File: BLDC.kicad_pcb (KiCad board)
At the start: 4 copper layers, 60 x 60 mm, 131 parts, among them J1 43650-0510, J2 436500313, J3 DNP, J4 43650-0510, J5 BONUS, U1 LMZ21700SIL, U12 MCP9808, U13 AS5047U, U17 INA250, U18 INA250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

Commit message: a bit of trivial cleanup. sent out for quote
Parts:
- moved TP3 0.42 mm to (151.1, 99.9)
- moved TP4 0.28 mm to (149.5, 98.6)
- moved TP6 0.14 mm to (146.5, 98.4)
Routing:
- net GND: track 138.8 -> 137.3 mm, vias 118 -> 119

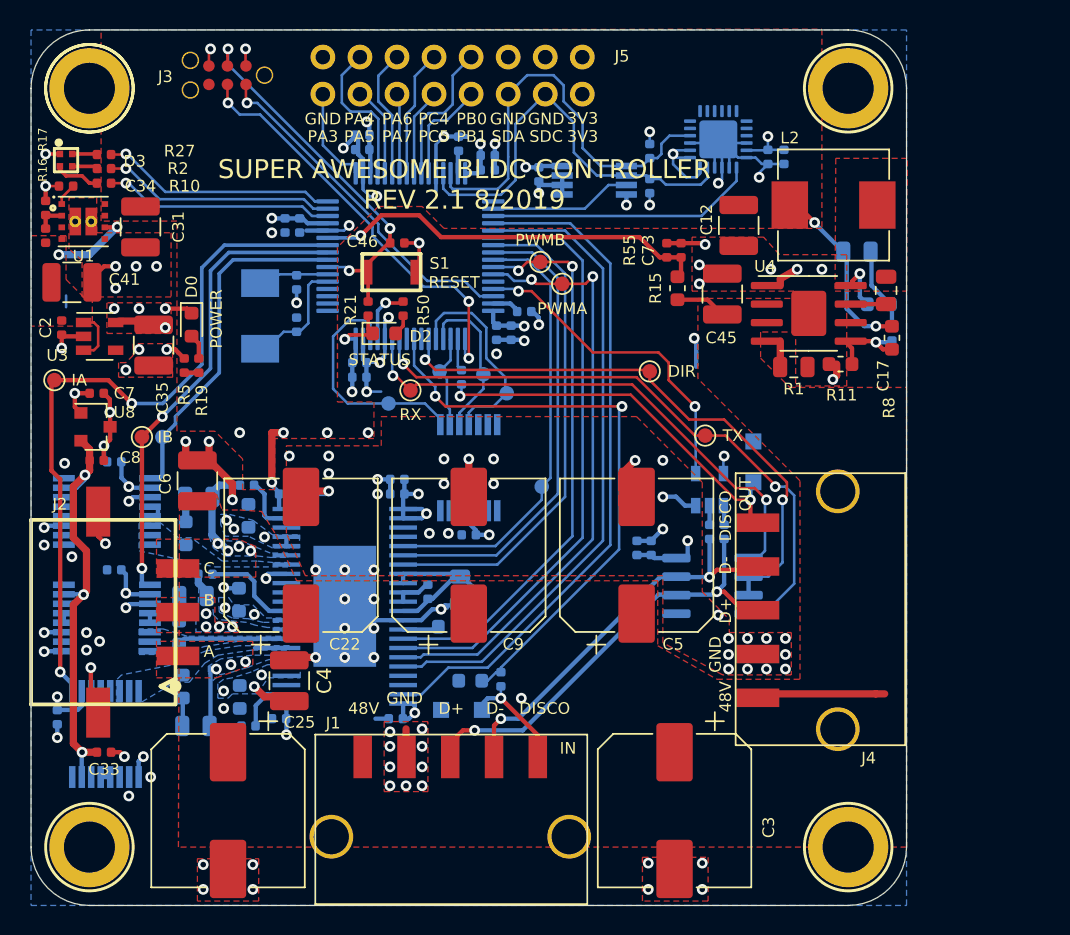
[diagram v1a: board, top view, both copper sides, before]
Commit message: WIP new revision, change INA250 to INA253 (higher bandwidth), regulator to low EMI version
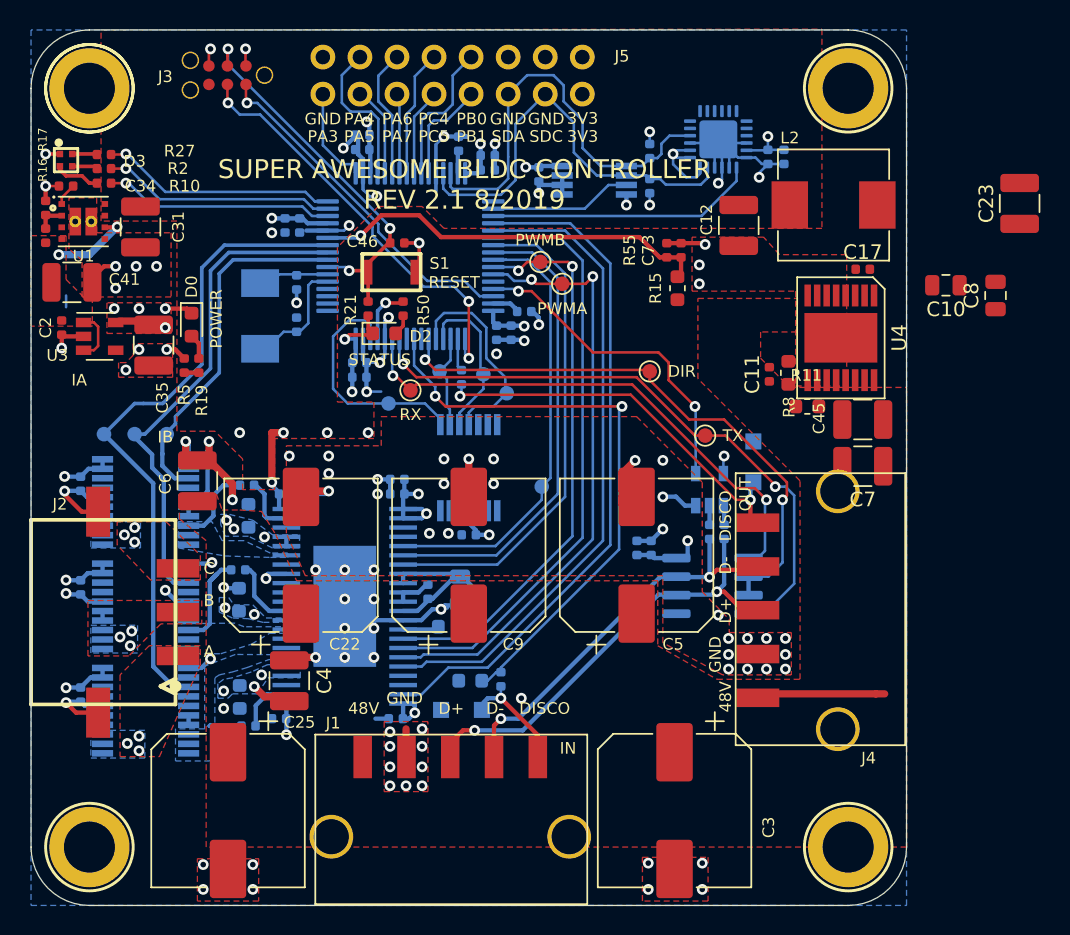
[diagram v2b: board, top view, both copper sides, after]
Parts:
- removed C28, C29: DNP, Capacitor_SMD:C_0603_1608Metric
- removed C33: 1u, Capacitor_SMD:C_0402_1005Metric
- removed R1: 40k2, Resistor_SMD:R_0805_2012Metric
- removed R12, R13, R14: DNP, Resistor_SMD:R_0805_2012Metric
- removed R7: 255k, Resistor_SMD:R_0603_1608Metric
- removed U17, U18, U19: INA250, Package_SO:TSSOP-16_4.4x5mm_P0.65mm
- removed U8: REF3312AIDBZ, Package_TO_SOT_SMD:SOT-23
- added U10: INA253, Package_SO:TSSOP-20_4.4x6.5mm_P0.65mm, B.Cu at (126.3, 121.7)
- added U11: INA253, Package_SO:TSSOP-20_4.4x6.5mm_P0.65mm, B.Cu at (126.3, 114.5)
- added U14: INA253, Package_SO:TSSOP-20_4.4x6.5mm_P0.65mm, B.Cu at (126.3, 107.3)
- C10: value 47p -> 2u2; footprint Capacitor_SMD:C_0402_1005Metric -> Capacitor_SMD:C_0805_2012Metric; moved to F.Cu
- C11: value 2n2 -> 82p; footprint Capacitor_SMD:C_0805_2012Metric -> Capacitor_SMD:C_0402_1005Metric; moved to F.Cu
- C17: value 2n2 -> 470n; footprint Capacitor_SMD:C_0805_2012Metric -> Capacitor_SMD:C_0402_1005Metric
- C23: value DNP -> 22u; footprint Capacitor_SMD:C_0603_1608Metric -> Capacitor_SMD:C_1210_3225Metric; moved to F.Cu
- C7: value 100n -> 4u7; footprint Capacitor_SMD:C_0402_1005Metric -> Capacitor_SMD:C_1210_3225Metric
- C8: value 1u -> 4u7; footprint Capacitor_SMD:C_0402_1005Metric -> Capacitor_SMD:C_0805_2012Metric
- L2: value 82u -> 100u
- R11: value 49k9 -> 92k
- R8: value 453k -> 1M
- TP11, TP12: moved to B.Cu
- U4: value LM5163 -> LM46000; footprint Package_SO:SOIC-8-1EP_3.9x4.9mm_P1.27mm_EP2.41x3.3mm -> BLDC:PWP0016G
- moved C8 62.6 mm to (184.6, 93.2), turned to 90 degrees
- moved C23 61.5 mm to (186.2, 86.9), turned to 90 degrees
- moved C7 52.7 mm to (175.5, 104.9)
- moved C45 12.9 mm to (175.5, 101.7), turned to 180 degrees
- moved C11 10.3 mm to (169.1, 98.6), turned to 90 degrees
- moved R8 7.49 mm to (170.4, 98.5)
- moved TP11 5.02 mm to (123.5, 102.7)
- moved C10 4.96 mm to (181.2, 92.5), turned to 180 degrees
- moved R11 3.69 mm to (171.7, 100.8), turned to 0 degrees
- moved U4 2.77 mm to (174.0, 96.1), turned to 180 degrees
- moved C13 2.75 mm to (121.9, 106.1), turned to 90 degrees
- moved C14 2.59 mm to (121.9, 113.2), turned to 90 degrees
- moved C53 2.27 mm to (132.7, 112.0)
- moved C16 2.23 mm to (121.9, 120.5)
- moved C17 2.16 mm to (175.5, 91.4), turned to 0 degrees
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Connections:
- C10 pad 2: Net-(C10-Pad2) -> GND
- C11 pad 1: +12V -> Net-(C11-Pad1)
- C11 pad 2: Net-(C10-Pad1) -> +12V
- C23 pad 1: Net-(C23-Pad1) -> +12V
- C23 pad 2: /GND_C -> GND
- C7 pad 2: +3V3 -> +48V
- C8 pad 1: GND -> +12V
- C8 pad 2: +1V2 -> GND
- J2 pad 1: /driver_phase-A -> /motor_phase-A
- J2 pad 2: /driver_phase-B -> /motor_phase-B
- J2 pad 3: /driver_phase-C -> /motor_phase-C
- L2 pad 1: Net-(C17-Pad1) -> Net-(C17-Pad2)
- R11 pad 1: Net-(C10-Pad2) -> Net-(C11-Pad1)
- R8 pad 2: Net-(C10-Pad2) -> Net-(C11-Pad1)
- U4 pad 1: GND -> Net-(C17-Pad2)
- U4 pad 2: +48V -> Net-(C17-Pad2)
- U4 pad 3: +48V -> Net-(C17-Pad1)
- U4 pad 4: Net-(R1-Pad1) -> Net-(C10-Pad1)
- U4 pad 5: Net-(C10-Pad2) -> +12V
- U4 pad 6: Net-(U4-Pad6) -> GND
- U4 pad 7: Net-(C17-Pad2) -> Net-(U4-Pad7)
- U4 pad 8: Net-(C17-Pad1) -> Net-(U4-Pad8)
- U4 pad 9: GND -> Net-(C11-Pad1)
- U5 pad 29: /GND_A -> GND
- U5 pad 30: /GND_B -> GND
- U5 pad 38: /GND_C -> GND
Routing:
- net +1V2: track 29.1 -> 0.00 mm, vias 3 -> 0
- net +12V: track 31.3 -> 19.1 mm, vias 11 -> 9
- net /GND_B: track 7.50 -> 0.00 mm
- net Net-(C10-Pad2): track 5.85 -> 0.00 mm, vias 1 -> 0
- net Net-(C10-Pad1): track 5.39 -> 0.00 mm
- net /driver_phase-B: track 1.69 -> 6.99 mm, vias 4 -> 0
- net /ISENSE_A: track 49.7 -> 44.9 mm, vias 2 -> 0
- net /driver_phase-A: track 6.20 -> 2.27 mm, vias 3 -> 0
- net +3V3: track 64.6 -> 61.0 mm, vias 24 -> 23
- net GND: track 137.3 -> 133.7 mm, vias 119 -> 100
- net +48V: track 15.1 -> 11.6 mm
- net Net-(C17-Pad1): track 3.34 -> 0.00 mm, vias 1 -> 0
- net Net-(C17-Pad2): track 2.20 -> 0.00 mm
- net /GND_A: track 2.16 -> 0.00 mm
- net Net-(C29-Pad1): track 1.93 -> 0.00 mm
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- added copper zone on F.Cu, net (none)
- added copper zone on B.Cu, net /motor_phase-A
- added copper zone on F.Cu, net /motor_phase-A
- added copper zone on B.Cu, net /motor_phase-B
- added copper zone on F.Cu, net /motor_phase-B
- added copper zone on B.Cu, net /motor_phase-C
- added copper zone on F.Cu, net /motor_phase-C
- removed copper zone on B.Cu, net /GND_A
- removed copper zone on B.Cu, net /GND_B
- removed copper zone on B.Cu, net /GND_C
- removed copper zone on F.Cu, net /driver_phase-A
- removed copper zone on F.Cu, net /driver_phase-B
- removed copper zone on F.Cu, net /driver_phase-C
- removed copper zone on F.Cu, net Net-(C17-Pad1)

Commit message: tinker with layout, mostly with 12v dc-dc
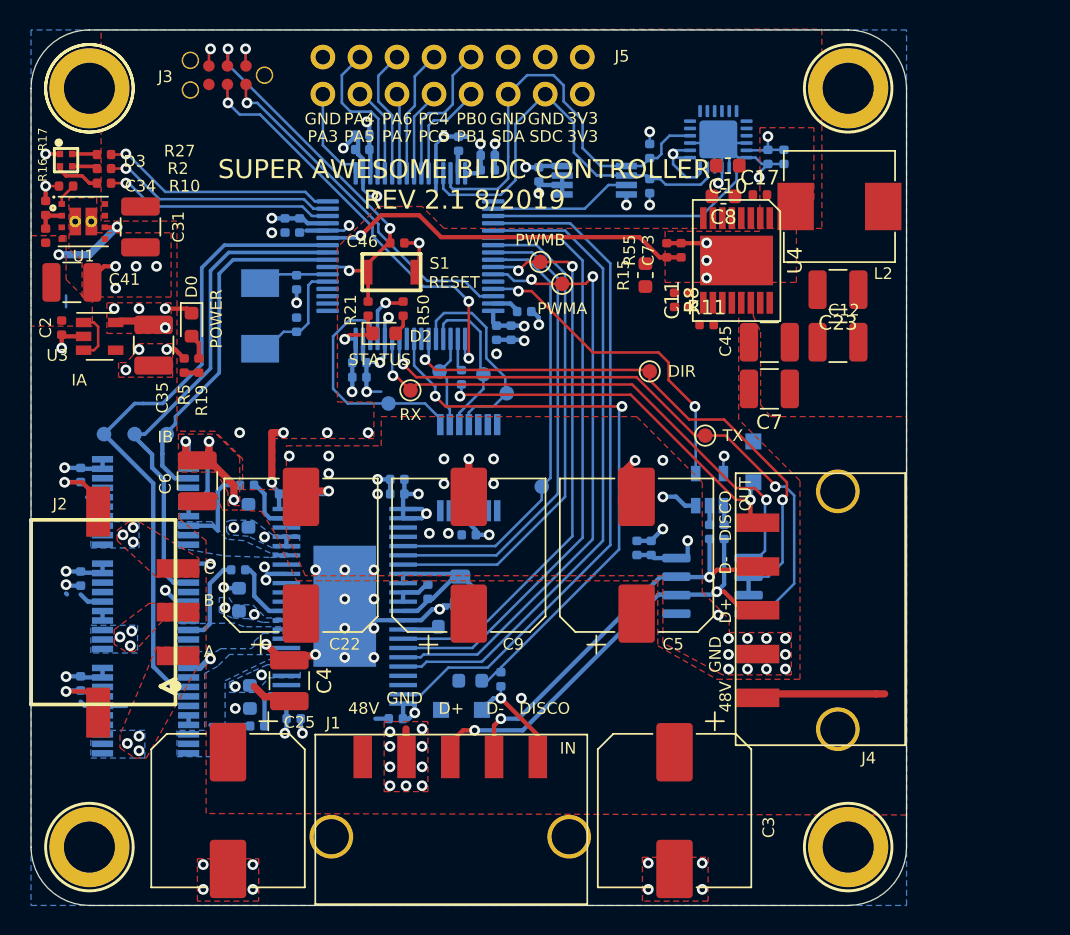
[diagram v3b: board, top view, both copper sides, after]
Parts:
- C10: footprint Capacitor_SMD:C_0805_2012Metric -> Capacitor_SMD:C_0603_1608Metric
- C8: value 4u7 -> 2u2; footprint Capacitor_SMD:C_0805_2012Metric -> Capacitor_SMD:C_0603_1608Metric
- R11, R8: footprint Resistor_SMD:R_0603_1608Metric -> Resistor_SMD:R_0402_1005Metric
- moved C8 19.8 mm to (166.0, 86.4), turned to 180 degrees
- moved C10 17.1 mm to (166.3, 84.3)
- moved C23 13.8 mm to (173.8, 92.8), turned to 180 degrees
- moved C12 10.5 mm to (173.8, 96.4), turned to 180 degrees
- moved R8 9.26 mm to (162.6, 93.5)
- moved U4 8.90 mm to (166.9, 90.8)
- moved R11 8.89 mm to (164.8, 95.2)
- moved C17 8.70 mm to (168.5, 86.3)
- moved C7 8.31 mm to (169.1, 99.6)
- moved C45 8.31 mm to (169.1, 96.4)
- moved C11 7.50 mm to (163.6, 93.5)
- moved R15 2.38 mm to (160.6, 91.8)
- moved C52 1.00 mm to (136.5, 122.2), turned to 180 degrees
- moved C16 0.77 mm to (121.9, 119.8)
- moved C1 0.70 mm to (133.5, 120.7)
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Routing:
- net GND: track 133.7 -> 140.7 mm, vias 100 -> 103
- net /VSENSE_VIN: track 27.6 -> 26.1 mm
- net /driver_phase-C: track 5.49 -> 6.52 mm
- net /driver_phase-B: track 6.99 -> 6.23 mm
- net +3V3: track 61.0 -> 60.3 mm
- net +48V: vias 8 -> 6
- removed copper zone on F.Cu, net (none)

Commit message: Added 3d model for regulator, routed all design (passing DRC)
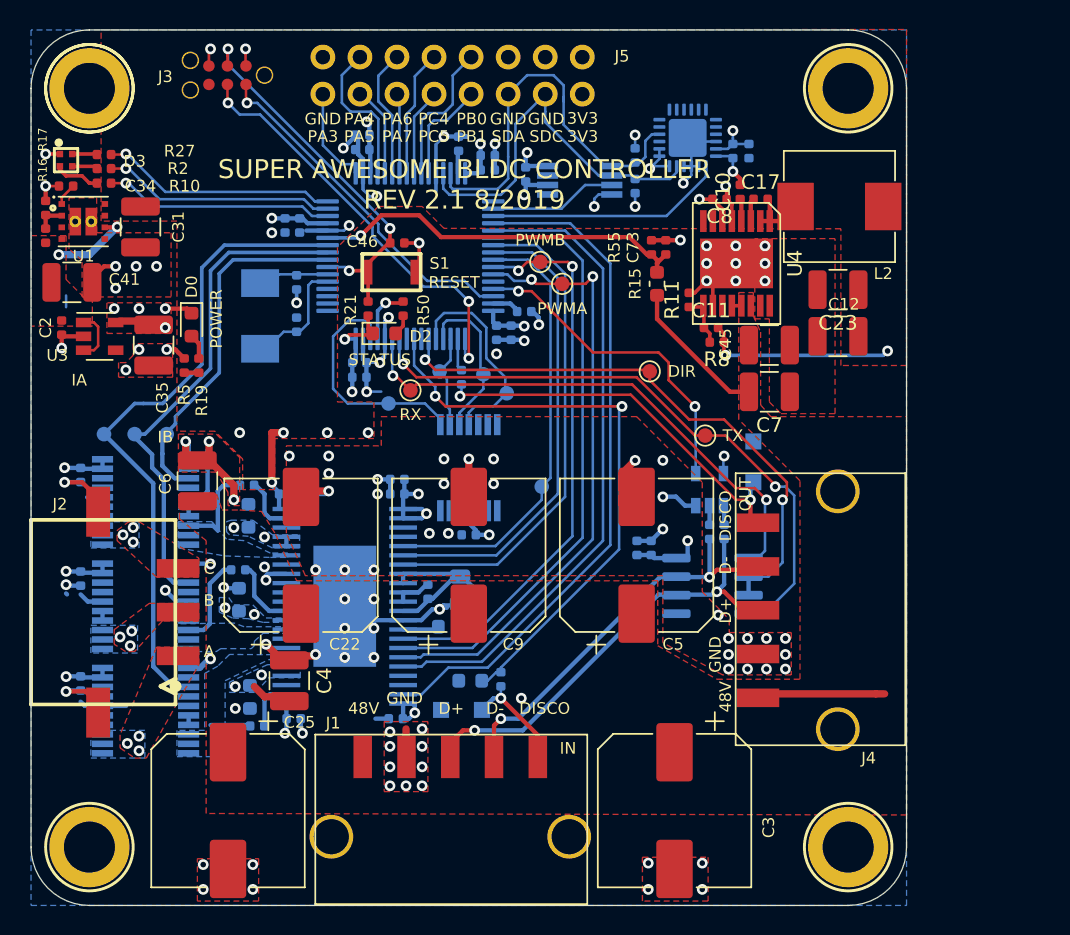
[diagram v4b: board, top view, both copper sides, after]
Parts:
- C10, C8: footprint Capacitor_SMD:C_0603_1608Metric -> Capacitor_SMD:C_0402_1005Metric
- moved R8 4.10 mm to (165.5, 96.4), turned to 180 degrees
- moved C20 2.43 mm to (167.7, 83.3)
- moved C21 2.43 mm to (166.6, 83.3)
- moved C11 2.42 mm to (165.1, 95.4), turned to 0 degrees
- moved U2 2.10 mm to (163.5, 82.4)
- moved R11 2.08 mm to (163.6, 93.5), turned to 90 degrees
- moved C10 1.99 mm to (167.1, 86.1), turned to 90 degrees
- moved C73 1.07 mm to (162.0, 89.9)
- moved R55 1.07 mm to (161.0, 89.9)
- moved R39 1.04 mm to (159.9, 83.6)
- moved R15 1.00 mm to (161.4, 92.4)
- moved R9 1.00 mm to (159.9, 85.7)
- moved U12 1.00 mm to (156.1, 85.3)
- moved C39 0.90 mm to (152.4, 84.9)
- moved C12 0.40 mm to (173.8, 96.0)
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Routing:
- net +12V: track 19.0 -> 34.9 mm, vias 9 -> 12
- net +48V: track 11.6 -> 22.2 mm
- net Net-(C17-Pad2): track 0.00 -> 4.40 mm
- net Net-(C11-Pad1): track 0.00 -> 3.69 mm
- net +3V3: track 60.3 -> 57.2 mm
- net /I2C_SCL: track 29.1 -> 26.5 mm
- net /IMU_INT1: track 18.6 -> 16.4 mm
- net GND: track 140.7 -> 138.6 mm, vias 103 -> 111
- net /I2C_SDA: track 29.7 -> 27.9 mm
- net Net-(C17-Pad1): track 0.00 -> 1.58 mm
- net Net-(C10-Pad1): track 0.00 -> 1.55 mm
- net /TEMP_INT: track 9.80 -> 8.80 mm
- net /VSENSE_VIN: track 26.1 -> 26.9 mm

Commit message: place/route tweaks. move accelerometer to top layer.
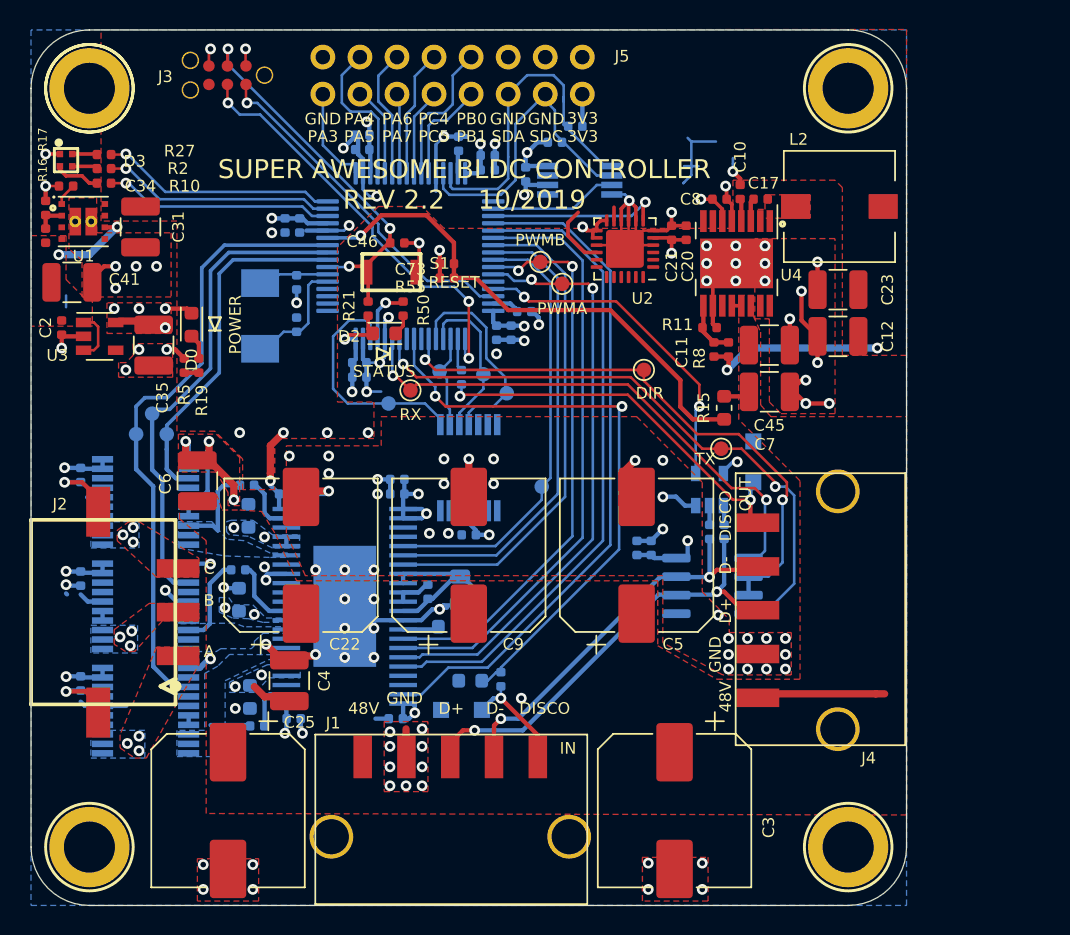
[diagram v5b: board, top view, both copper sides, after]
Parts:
- C20, C21, U2: moved to F.Cu
- moved C73 15.0 mm to (147.0, 91.0), turned to 0 degrees
- moved R55 14.2 mm to (147.0, 92.0), turned to 180 degrees
- moved R15 9.66 mm to (166.0, 100.9), turned to -90 degrees
- moved U2 8.73 mm to (159.2, 90.0)
- moved C20 7.06 mm to (163.4, 88.9), turned to -90 degrees
- moved C21 7.00 mm to (162.4, 88.9), turned to -90 degrees
- moved R9 6.26 mm to (154.4, 82.7), turned to 180 degrees
- moved R39 4.56 mm to (155.8, 81.6), turned to 0 degrees
- moved R11 2.36 mm to (165.0, 95.4), turned to 0 degrees
- moved TP11 2.20 mm to (125.7, 102.7)
- moved TP12 1.84 mm to (126.8, 101.3)
- moved C11 1.51 mm to (165.3, 96.9), turned to -90 degrees
- moved TP7 1.42 mm to (165.8, 103.7)
- moved R8 0.94 mm to (166.3, 96.9), turned to 90 degrees
- moved TP8 0.41 mm to (160.5, 98.3)
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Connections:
- D0 pad 1: +3V3 -> Net-(D0-Pad1)
- D0 pad 2: Net-(D0-Pad2) -> +3V3
- D2 pad 1: +3V3 -> Net-(D2-Pad1)
- D2 pad 2: Net-(D2-Pad2) -> +3V3
- R19 pad 1: Net-(D0-Pad2) -> Net-(D0-Pad1)
- R50 pad 1: Net-(D2-Pad2) -> Net-(D2-Pad1)
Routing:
- net GND: track 138.6 -> 170.1 mm, vias 111 -> 118
- net /VSENSE_VIN: track 26.9 -> 36.2 mm
- net +48V: track 22.2 -> 14.1 mm
- net /IMU_INT1: track 16.4 -> 12.1 mm, vias 0 -> 1
- net /I2C_SCL: track 26.5 -> 22.3 mm
- net Net-(C17-Pad2): track 4.40 -> 1.32 mm
- net /ISENSE_A: track 44.9 -> 42.9 mm
- net +3V3: track 57.2 -> 59.1 mm, vias 23 -> 21
- net Net-(D0-Pad2): track 1.73 -> 0.00 mm
- net Net-(D0-Pad1): track 0.00 -> 1.73 mm
- net Net-(D2-Pad2): track 1.53 -> 0.00 mm
- net Net-(D2-Pad1): track 0.00 -> 1.53 mm
- net /MOT_PWM_A: track 42.0 -> 40.9 mm
- net /ISENSE_B: track 34.8 -> 33.6 mm
- net +12V: track 34.9 -> 34.1 mm
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- added copper zone on F.Cu, net Net-(C17-Pad2)
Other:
- board text added: "SUPER AWESOME BLDC CONTROLLER REV 2.2 10/2019"
- board text removed: "SUPER AWESOME BLDC CONTROLLER REV 2.1 8/2019"

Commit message: Routed I2C, updated BOM
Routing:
- net /I2C_SDA: track 27.4 -> 34.4 mm, vias 0 -> 1
- net /I2C_SCL: track 22.3 -> 26.6 mm, vias 0 -> 1
